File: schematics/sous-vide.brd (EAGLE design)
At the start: 81.3 x 81.3 mm, 30 parts, among them IC1 MEGA32-P

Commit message: Average temp reading + ISP connector
Temp readings are averaged per second before comparing to the set
temperature. Added ISP header to board for on-board reprogramming.
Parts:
- added JP9: (no value), pinhead:2X03
- turned R5 to 180 degrees
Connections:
- new net N$17: IC1.8, JP9.3
- net GND: now also JP9.6
- net N$11: now also JP9.4
- net N$13: now also JP9.1
- net N$3: now also JP9.5
- net VCC: now also JP9.2
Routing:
- net N$11: track 24.2 -> 84.7 mm
- net N$3: track 10.2 -> 58.7 mm
- net N$17: track 0.00 -> 48.6 mm
- net N$13: track 39.5 -> 88.0 mm
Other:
- board text added: "1"
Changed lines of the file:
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@@
 <text x="78.105" y="72.39" size="1.778" layer="16" rot="MR0">0</text>
 <text x="75.565" y="72.39" size="1.778" layer="16" rot="MR0">+</text>
+<text x="15.24" y="67.31" size="1.778" layer="16" rot="MR270">1</text>
 </plain>
 <attributes>
@@
 <element name="R4" library="rcl" package="0207/2V" value="330" x="55.88" y="15.24"/>
 <element name="C1" library="resistor" package="C025-025X050" value="" x="38.1" y="66.04" rot="R180"/>
-<element name="R5" library="resistor" package="RTRIM3339P" value="" x="5.08" y="55.88" rot="R90"/>
+<element name="R5" library="resistor" package="RTRIM3339P" value="" x="5.08" y="55.88" rot="R180"/>
 <element name="R6" library="rcl" package="0207/2V" value="330" x="45.72" y="73.66"/>
 <element name="H1" library="holes" package="3,0" value="MOUNT-HOLE3.0" x="76.2" y="5.08"/>
@@
 <element name="H3" library="holes" package="3,0" value="MOUNT-HOLE3.0" x="76.2" y="40.64"/>
 <element name="H4" library="holes" package="3,0" value="MOUNT-HOLE3.0" x="5.08" y="5.08"/>
+<element name="JP9" library="pinhead" package="2X03" value="" x="11.43" y="69.85" rot="MR0"/>
 </elements>
 <signals>
@@
 <contactref element="S7" pad="4"/>
 <contactref element="S4" pad="4"/>
+<contactref element="JP9" pad="6"/>
 </signal>
 <signal name="N$3">
@@
 <contactref element="R1" pad="2"/>
 <wire x1="39.37" y1="48.26" x2="39.37" y2="38.1" width="0.4064" layer="16"/>
+<contactref element="JP9" pad="5"/>
+<wire x1="8.89" y1="68.58" x2="8.89" y2="67.31" width="0.4064" layer="1"/>
+<wire x1="8.89" y1="67.31" x2="10.16" y2="66.04" width="0.4064" layer="1"/>
+<wire x1="10.16" y1="66.04" x2="10.16" y2="53.34" width="0.4064" layer="1"/>
+<wire x1="10.16" y1="53.34" x2="11.43" y2="52.07" width="0.4064" layer="1"/>
+<wire x1="11.43" y1="52.07" x2="38.1" y2="52.07" width="0.4064" layer="1"/>
+<wire x1="38.1" y1="52.07" x2="39.37" y2="50.8" width="0.4064" layer="1"/>
+<wire x1="39.37" y1="50.8" x2="39.37" y2="48.26" width="0.4064" layer="1"/>
 </signal>
 <signal name="VCC">
@@
 <contactref element="R5" pad="1"/>
 <contactref element="R6" pad="2"/>
+<contactref element="JP9" pad="2"/>
 </signal>
 <signal name="N$12">
@@
 <wire x1="52.07" y1="35.56" x2="46.99" y2="40.64" width="0.4064" layer="16"/>
 <wire x1="46.99" y1="40.64" x2="46.99" y2="48.26" width="0.4064" layer="16"/>
+<contactref element="JP9" pad="4"/>
+<wire x1="46.99" y1="48.26" x2="46.99" y2="54.61" width="0.4064" layer="1"/>
+<wire x1="46.99" y1="54.61" x2="45.72" y2="55.88" width="0.4064" layer="1"/>
+<wire x1="45.72" y1="55.88" x2="19.05" y2="55.88" width="0.4064" layer="1"/>
+<wire x1="19.05" y1="55.88" x2="17.78" y2="57.15" width="0.4064" layer="1"/>
+<wire x1="17.78" y1="57.15" x2="17.78" y2="72.39" width="0.4064" layer="1"/>
+<wire x1="17.78" y1="72.39" x2="16.51" y2="73.66" width="0.4064" layer="1"/>
+<wire x1="16.51" y1="73.66" x2="12.7" y2="73.66" width="0.4064" layer="1"/>
+<wire x1="12.7" y1="73.66" x2="11.43" y2="72.39" width="0.4064" layer="1"/>
+<wire x1="11.43" y1="72.39" x2="11.43" y2="71.12" width="0.4064" layer="1"/>
 </signal>
 <signal name="N$13">
@@
 <wire x1="44.45" y1="48.26" x2="44.45" y2="39.37" width="0.4064" layer="16"/>
 <wire x1="44.45" y1="39.37" x2="49.53" y2="34.29" width="0.4064" layer="16"/>
+<contactref element="JP9" pad="1"/>
+<wire x1="13.97" y1="68.58" x2="13.97" y2="67.31" width="0.4064" layer="1"/>
+<wire x1="13.97" y1="67.31" x2="15.24" y2="66.04" width="0.4064" layer="1"/>
+<wire x1="15.24" y1="66.04" x2="15.24" y2="55.88" width="0.4064" layer="1"/>
+<wire x1="15.24" y1="55.88" x2="16.51" y2="54.61" width="0.4064" layer="1"/>
+<wire x1="16.51" y1="54.61" x2="43.18" y2="54.61" width="0.4064" layer="1"/>
+<wire x1="43.18" y1="54.61" x2="44.45" y2="53.34" width="0.4064" layer="1"/>
+<wire x1="44.45" y1="53.34" x2="44.45" y2="48.26" width="0.4064" layer="1"/>
 </signal>
 <signal name="N$14">
@@
 <wire x1="13.97" y1="76.2" x2="13.97" y2="74.93" width="0.4064" layer="16"/>
 <wire x1="13.97" y1="74.93" x2="12.7" y2="73.66" width="0.4064" layer="16"/>
-<wire x1="12.7" y1="73.66" x2="8.89" y2="73.66" width="0.4064" layer="16"/>
-<wire x1="8.89" y1="73.66" x2="7.62" y2="72.39" width="0.4064" layer="16"/>
-<wire x1="7.62" y1="72.39" x2="7.62" y2="55.88" width="0.4064" layer="16"/>
+<wire x1="12.7" y1="73.66" x2="6.35" y2="73.66" width="0.4064" layer="16"/>
+<wire x1="6.35" y1="73.66" x2="5.08" y2="72.39" width="0.4064" layer="16"/>
+<wire x1="5.08" y1="72.39" x2="5.08" y2="58.42" width="0.4064" layer="16"/>
 </signal>
 <signal name="N$15">
@@
 <wire x1="44.45" y1="73.66" x2="44.45" y2="76.2" width="0.4064" layer="16"/>
 </signal>
+<signal name="N$17">
+<contactref element="JP9" pad="3"/>
+<contactref element="IC1" pad="8"/>
+<wire x1="12.7" y1="54.61" x2="13.97" y2="53.34" width="0.4064" layer="1"/>
+<wire x1="13.97" y1="53.34" x2="40.64" y2="53.34" width="0.4064" layer="1"/>
+<wire x1="40.64" y1="53.34" x2="41.91" y2="52.07" width="0.4064" layer="1"/>
+<wire x1="41.91" y1="52.07" x2="41.91" y2="48.26" width="0.4064" layer="1"/>
+<wire x1="12.7" y1="54.61" x2="12.7" y2="66.04" width="0.4064" layer="1"/>
+<wire x1="12.7" y1="66.04" x2="11.43" y2="67.31" width="0.4064" layer="1"/>
+<wire x1="11.43" y1="67.31" x2="11.43" y2="68.58" width="0.4064" layer="1"/>
+</signal>
 </signals>

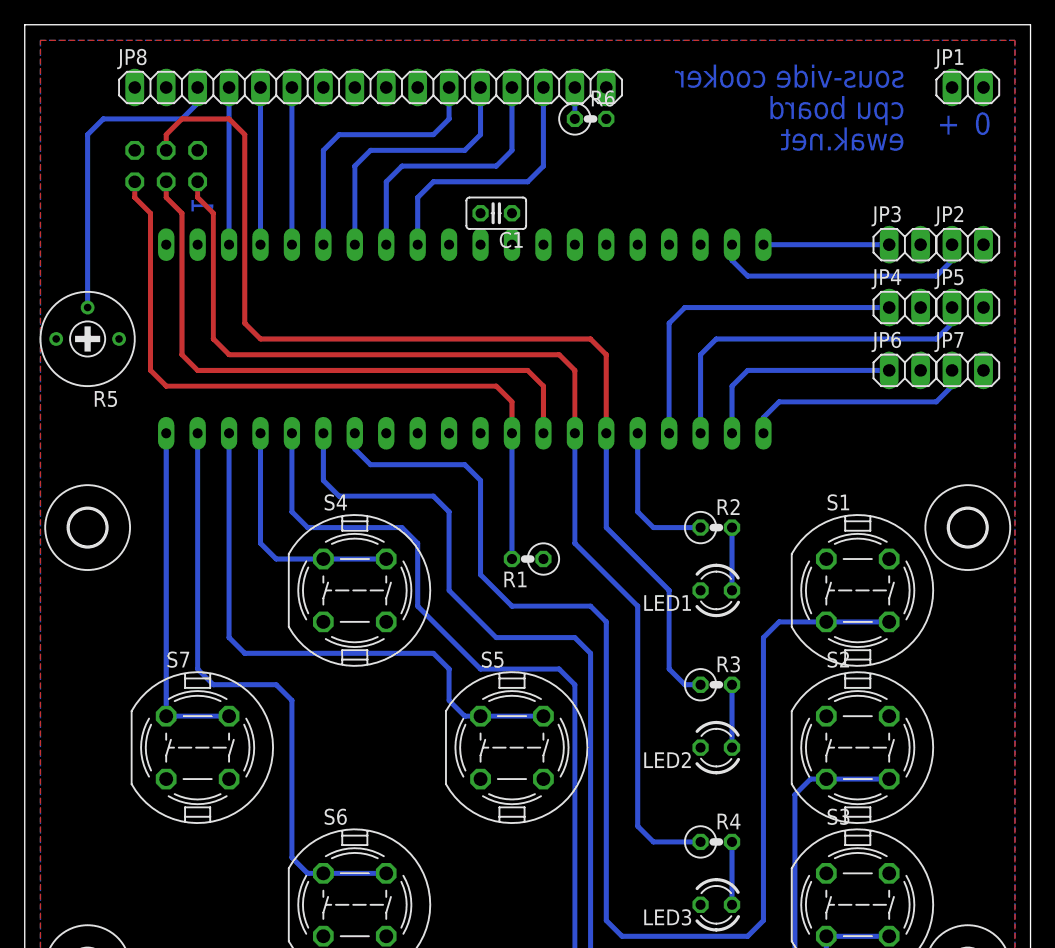
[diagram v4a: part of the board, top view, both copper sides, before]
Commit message: Updated schematic and PCB
Now includes 4th led for reading indicator. Moved ISP connector to more
accessible location.
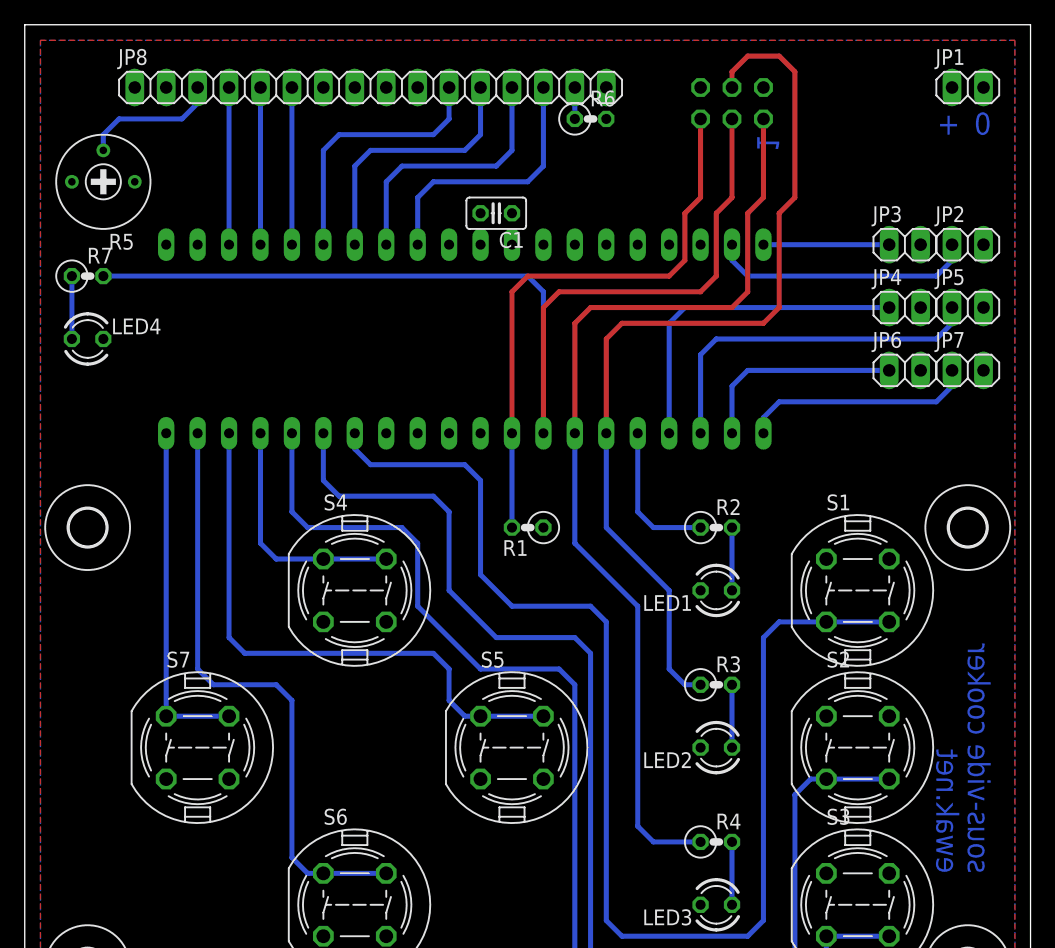
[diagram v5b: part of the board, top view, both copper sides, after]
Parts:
- added LED4: (no value), led:LED3MM
- added R7: 330, rcl:0207/2V
- JP9: value (none) -> ISP
- moved JP9 46.0 mm to (57.1, 74.9)
- moved R5 12.8 mm to (6.35, 68.6)
- moved R1 2.54 mm to (40.6, 40.6)
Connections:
- new net N$16: LED4.A, R7.1
- net GND: now also LED4.K
- net N$17: now also R7.2
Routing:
- net N$17: track 48.6 -> 85.9 mm
- net N$14: track 25.2 -> 11.2 mm
- net N$3: track 58.7 -> 46.0 mm
- net N$11: track 84.7 -> 73.8 mm
- net N$13: track 88.0 -> 77.9 mm
- net N$16: track 0.00 -> 5.08 mm
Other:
- board text removed: "cpu board"
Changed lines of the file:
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@@
 <wire x1="81.27" y1="81.27" x2="0" y2="81.27" width="0" layer="20"/>
 <wire x1="0" y1="81.27" x2="0" y2="0" width="0" layer="20"/>
-<text x="71.12" y="76.2" size="1.778" layer="16" rot="MR0">sous-vide cooker</text>
-<text x="71.12" y="71.12" size="1.778" layer="16" rot="MR0">ewak.net</text>
-<text x="71.12" y="73.66" size="1.778" layer="16" rot="MR0">cpu board</text>
+<text x="76.2" y="12.7" size="1.778" layer="16" rot="MR90">sous-vide cooker</text>
+<text x="73.66" y="12.7" size="1.778" layer="16" rot="MR90">ewak.net</text>
 <text x="78.105" y="72.39" size="1.778" layer="16" rot="MR0">0</text>
 <text x="75.565" y="72.39" size="1.778" layer="16" rot="MR0">+</text>
-<text x="15.24" y="67.31" size="1.778" layer="16" rot="MR270">1</text>
+<text x="60.96" y="72.39" size="1.778" layer="16" rot="MR270">1</text>
 </plain>
 <attributes>
@@
 <attribute name="OC_FARNELL" value="1661729" x="-3.81" y="6.35" size="1.778" layer="28" rot="MR0" display="off"/>
 </element>
-<element name="R1" library="rcl" package="0207/2V" value="100k" x="40.64" y="38.1" rot="R180"/>
+<element name="R1" library="rcl" package="0207/2V" value="100k" x="40.64" y="40.64" rot="R180"/>
 <element name="JP8" library="pinhead" package="1X16" value="display" x="27.94" y="76.2"/>
 <element name="S1" library="switch-misc" package="DT6" value="DT6" x="67.31" y="35.56"/>
@@
 <element name="R4" library="rcl" package="0207/2V" value="330" x="55.88" y="15.24"/>
 <element name="C1" library="resistor" package="C025-025X050" value="" x="38.1" y="66.04" rot="R180"/>
-<element name="R5" library="resistor" package="RTRIM3339P" value="" x="5.08" y="55.88" rot="R180"/>
+<element name="R5" library="resistor" package="RTRIM3339P" value="" x="6.35" y="68.58" rot="R180"/>
 <element name="R6" library="rcl" package="0207/2V" value="330" x="45.72" y="73.66"/>
 <element name="H1" library="holes" package="3,0" value="MOUNT-HOLE3.0" x="76.2" y="5.08"/>
@@
 <element name="H3" library="holes" package="3,0" value="MOUNT-HOLE3.0" x="76.2" y="40.64"/>
 <element name="H4" library="holes" package="3,0" value="MOUNT-HOLE3.0" x="5.08" y="5.08"/>
-<element name="JP9" library="pinhead" package="2X03" value="" x="11.43" y="69.85" rot="MR0"/>
+<element name="JP9" library="pinhead" package="2X03" value="ISP" x="57.15" y="74.93" rot="MR0"/>
+<element name="LED4" library="led" package="LED3MM" value="" x="5.08" y="55.88"/>
+<element name="R7" library="rcl" package="0207/2V" value="330" x="5.08" y="60.96"/>
 </elements>
 <signals>
@@
 <contactref element="S4" pad="4"/>
 <contactref element="JP9" pad="6"/>
+<contactref element="LED4" pad="K"/>
 </signal>
 <signal name="N$3">
 <contactref element="IC1" pad="9"/>
 <contactref element="R1" pad="2"/>
-<wire x1="39.37" y1="48.26" x2="39.37" y2="38.1" width="0.4064" layer="16"/>
+<wire x1="39.37" y1="48.26" x2="39.37" y2="40.64" width="0.4064" layer="16"/>
 <contactref element="JP9" pad="5"/>
-<wire x1="8.89" y1="68.58" x2="8.89" y2="67.31" width="0.4064" layer="1"/>
-<wire x1="8.89" y1="67.31" x2="10.16" y2="66.04" width="0.4064" layer="1"/>
-<wire x1="10.16" y1="66.04" x2="10.16" y2="53.34" width="0.4064" layer="1"/>
-<wire x1="10.16" y1="53.34" x2="11.43" y2="52.07" width="0.4064" layer="1"/>
-<wire x1="11.43" y1="52.07" x2="38.1" y2="52.07" width="0.4064" layer="1"/>
-<wire x1="38.1" y1="52.07" x2="39.37" y2="50.8" width="0.4064" layer="1"/>
-<wire x1="39.37" y1="50.8" x2="39.37" y2="48.26" width="0.4064" layer="1"/>
+<wire x1="54.61" y1="73.66" x2="54.61" y2="67.31" width="0.4064" layer="1"/>
+<wire x1="54.61" y1="67.31" x2="53.34" y2="66.04" width="0.4064" layer="1"/>
+<wire x1="53.34" y1="66.04" x2="53.34" y2="62.23" width="0.4064" layer="1"/>
+<wire x1="53.34" y1="62.23" x2="52.07" y2="60.96" width="0.4064" layer="1"/>
+<wire x1="52.07" y1="60.96" x2="40.64" y2="60.96" width="0.4064" layer="1"/>
+<wire x1="40.64" y1="60.96" x2="39.37" y2="59.69" width="0.4064" layer="1"/>
+<wire x1="39.37" y1="59.69" x2="39.37" y2="48.26" width="0.4064" layer="1"/>
 </signal>
 <signal name="VCC">
@@
 <wire x1="46.99" y1="40.64" x2="46.99" y2="48.26" width="0.4064" layer="16"/>
 <contactref element="JP9" pad="4"/>
-<wire x1="46.99" y1="48.26" x2="46.99" y2="54.61" width="0.4064" layer="1"/>
-<wire x1="46.99" y1="54.61" x2="45.72" y2="55.88" width="0.4064" layer="1"/>
-<wire x1="45.72" y1="55.88" x2="19.05" y2="55.88" width="0.4064" layer="1"/>
-<wire x1="19.05" y1="55.88" x2="17.78" y2="57.15" width="0.4064" layer="1"/>
-<wire x1="17.78" y1="57.15" x2="17.78" y2="72.39" width="0.4064" layer="1"/>
-<wire x1="17.78" y1="72.39" x2="16.51" y2="73.66" width="0.4064" layer="1"/>
-<wire x1="16.51" y1="73.66" x2="12.7" y2="73.66" width="0.4064" layer="1"/>
-<wire x1="12.7" y1="73.66" x2="11.43" y2="72.39" width="0.4064" layer="1"/>
-<wire x1="11.43" y1="72.39" x2="11.43" y2="71.12" width="0.4064" layer="1"/>
+<wire x1="46.99" y1="48.26" x2="46.99" y2="55.88" width="0.4064" layer="1"/>
+<wire x1="46.99" y1="55.88" x2="48.26" y2="57.15" width="0.4064" layer="1"/>
+<wire x1="48.26" y1="57.15" x2="59.69" y2="57.15" width="0.4064" layer="1"/>
+<wire x1="59.69" y1="57.15" x2="60.96" y2="58.42" width="0.4064" layer="1"/>
+<wire x1="60.96" y1="58.42" x2="60.96" y2="66.04" width="0.4064" layer="1"/>
+<wire x1="60.96" y1="66.04" x2="62.23" y2="67.31" width="0.4064" layer="1"/>
+<wire x1="62.23" y1="67.31" x2="62.23" y2="77.47" width="0.4064" layer="1"/>
+<wire x1="62.23" y1="77.47" x2="60.96" y2="78.74" width="0.4064" layer="1"/>
+<wire x1="60.96" y1="78.74" x2="58.42" y2="78.74" width="0.4064" layer="1"/>
+<wire x1="58.42" y1="78.74" x2="57.15" y2="77.47" width="0.4064" layer="1"/>
+<wire x1="57.15" y1="77.47" x2="57.15" y2="76.2" width="0.4064" layer="1"/>
 </signal>
 <signal name="N$13">
@@
 <wire x1="44.45" y1="39.37" x2="49.53" y2="34.29" width="0.4064" layer="16"/>
 <contactref element="JP9" pad="1"/>
-<wire x1="13.97" y1="68.58" x2="13.97" y2="67.31" width="0.4064" layer="1"/>
-<wire x1="13.97" y1="67.31" x2="15.24" y2="66.04" width="0.4064" layer="1"/>
-<wire x1="15.24" y1="66.04" x2="15.24" y2="55.88" width="0.4064" layer="1"/>
-<wire x1="15.24" y1="55.88" x2="16.51" y2="54.61" width="0.4064" layer="1"/>
-<wire x1="16.51" y1="54.61" x2="43.18" y2="54.61" width="0.4064" layer="1"/>
-<wire x1="43.18" y1="54.61" x2="44.45" y2="53.34" width="0.4064" layer="1"/>
-<wire x1="44.45" y1="53.34" x2="44.45" y2="48.26" width="0.4064" layer="1"/>
+<wire x1="59.69" y1="73.66" x2="59.69" y2="67.31" width="0.4064" layer="1"/>
+<wire x1="59.69" y1="67.31" x2="58.42" y2="66.04" width="0.4064" layer="1"/>
+<wire x1="58.42" y1="66.04" x2="58.42" y2="59.69" width="0.4064" layer="1"/>
+<wire x1="58.42" y1="59.69" x2="57.15" y2="58.42" width="0.4064" layer="1"/>
+<wire x1="57.15" y1="58.42" x2="45.72" y2="58.42" width="0.4064" layer="1"/>
+<wire x1="45.72" y1="58.42" x2="44.45" y2="57.15" width="0.4064" layer="1"/>
+<wire x1="44.45" y1="57.15" x2="44.45" y2="48.26" width="0.4064" layer="1"/>
 </signal>
 <signal name="N$14">
@@
 <wire x1="13.97" y1="76.2" x2="13.97" y2="74.93" width="0.4064" layer="16"/>
 <wire x1="13.97" y1="74.93" x2="12.7" y2="73.66" width="0.4064" layer="16"/>
-<wire x1="12.7" y1="73.66" x2="6.35" y2="73.66" width="0.4064" layer="16"/>
-<wire x1="6.35" y1="73.66" x2="5.08" y2="72.39" width="0.4064" layer="16"/>
-<wire x1="5.08" y1="72.39" x2="5.08" y2="58.42" width="0.4064" layer="16"/>
+<wire x1="12.7" y1="73.66" x2="7.62" y2="73.66" width="0.4064" layer="16"/>
+<wire x1="7.62" y1="73.66" x2="6.35" y2="72.39" width="0.4064" layer="16"/>
+<wire x1="6.35" y1="72.39" x2="6.35" y2="71.12" width="0.4064" layer="16"/>
 </signal>
 <signal name="N$15">
@@
 <contactref element="JP9" pad="3"/>
 <contactref element="IC1" pad="8"/>
-<wire x1="12.7" y1="54.61" x2="13.97" y2="53.34" width="0.4064" layer="1"/>
-<wire x1="13.97" y1="53.34" x2="40.64" y2="53.34" width="0.4064" layer="1"/>
-<wire x1="40.64" y1="53.34" x2="41.91" y2="52.07" width="0.4064" layer="1"/>
-<wire x1="41.91" y1="52.07" x2="41.91" y2="48.26" width="0.4064" layer="1"/>
-<wire x1="12.7" y1="54.61" x2="12.7" y2="66.04" width="0.4064" layer="1"/>
-<wire x1="12.7" y1="66.04" x2="11.43" y2="67.31" width="0.4064" layer="1"/>
-<wire x1="11.43" y1="67.31" x2="11.43" y2="68.58" width="0.4064" layer="1"/>
+<contactref element="R7" pad="2"/>
+<wire x1="41.91" y1="48.26" x2="41.91" y2="58.42" width="0.4064" layer="1"/>
+<wire x1="41.91" y1="58.42" x2="43.18" y2="59.69" width="0.4064" layer="1"/>
+<wire x1="43.18" y1="59.69" x2="54.61" y2="59.69" width="0.4064" layer="1"/>
+<wire x1="54.61" y1="59.69" x2="55.88" y2="60.96" width="0.4064" layer="1"/>
+<wire x1="55.88" y1="60.96" x2="55.88" y2="66.04" width="0.4064" layer="1"/>
+<wire x1="55.88" y1="66.04" x2="57.15" y2="67.31" width="0.4064" layer="1"/>
+<wire x1="57.15" y1="67.31" x2="57.15" y2="73.66" width="0.4064" layer="1"/>
+<wire x1="6.35" y1="60.96" x2="40.64" y2="60.96" width="0.4064" layer="16"/>
+<wire x1="40.64" y1="60.96" x2="41.91" y2="59.69" width="0.4064" layer="16"/>
+<wire x1="41.91" y1="59.69" x2="41.91" y2="48.26" width="0.4064" layer="16"/>
+</signal>
+<signal name="N$16">
+<contactref element="R7" pad="1"/>
+<contactref element="LED4" pad="A"/>
+<wire x1="3.81" y1="60.96" x2="3.81" y2="55.88" width="0.4064" layer="16"/>
 </signal>
 </signals>
